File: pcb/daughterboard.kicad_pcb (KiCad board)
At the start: 2 copper layers, 18 parts, among them J1 USB_C_Receptacle_USB2.0, J2 Conn_01x02_Female, J3 Conn_01x02_Female, J4 USB_C_Receptacle_USB2.0, J5 Conn_01x02_Female, J6 Conn_01x02_Female

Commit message: cleanup
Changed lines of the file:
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@@
+    (effects (font (size 0.8 0.8) (thickness 0.15)) (justify mirror))
+  )
+  (gr_text "D-" (at 107.987816 57.802755 -15) (layer "B.SilkS")
     (effects (font (size 0.8 0.8) (thickness 0.15)) (justify mirror))
   )
   (gr_text "D-" (at 68.235 57.678152 -15) (layer "B.SilkS")
+    (effects (font (size 0.8 0.8) (thickness 0.15)) (justify mirror))
+  )
+  (gr_text "D+" (at 106.600608 59.953449 -15) (layer "B.SilkS")
     (effects (font (size 0.8 0.8) (thickness 0.15)) (justify mirror))
   )
@@
     (effects (font (size 0.8 0.8) (thickness 0.15)) (justify mirror))
   )
+  (gr_text "GND" (at 85.778968 58.419 -45) (layer "B.SilkS")
+    (effects (font (size 0.8 0.8) (thickness 0.15)) (justify mirror))
+  )
   (gr_text "Solder on this side" (at 56.16 62.303152) (layer "B.SilkS")
     (effects (font (size 1 1) (thickness 0.2)) (justify mirror))
+  )
+  (gr_text "VBUS" (at 85.55 55.89 -45) (layer "B.SilkS")
+    (effects (font (size 0.8 0.8) (thickness 0.15)) (justify mirror))
+  )
+  (gr_text "GND" (at 85.962816 59.454603 45) (layer "F.SilkS")
+    (effects (font (size 0.8 0.8) (thickness 0.15)))
   )
   (gr_text "Solder on this side" (at 97.61 62.24) (layer "F.SilkS")
@@
     (effects (font (size 1 1) (thickness 0.15)))
   )
+  (gr_text "VBUS" (at 85.733848 56.925603 45) (layer "F.SilkS")
+    (effects (font (size 0.8 0.8) (thickness 0.15)))
+  )
   (gr_text "GND" (at 46.21 59.33 45) (layer "F.SilkS")
     (effects (font (size 0.8 0.8) (thickness 0.15)))
@@
     (effects (font (size 0.8 0.8) (thickness 0.15)))
   )
+  (gr_text "D-" (at 108.312816 58.027755 15) (layer "F.SilkS")
+    (effects (font (size 0.8 0.8) (thickness 0.15)))
+  )
   (gr_text "VBUS" (at 45.981032 56.801 45) (layer "F.SilkS")
     (effects (font (size 0.8 0.8) (thickness 0.15)))
   )
   (gr_text "D+" (at 67.097208 59.978846 15) (layer "F.SilkS")
+    (effects (font (size 0.8 0.8) (thickness 0.15)))
+  )
+  (gr_text "D+" (at 106.850024 60.103449 15) (layer "F.SilkS")
     (effects (font (size 0.8 0.8) (thickness 0.15)))
   )
@@
   (segment (start 57.79 60.47) (end 57.79 58.385) (width 0.16) (layer "F.Cu") (net 7))
   (segment (start 57.88 60.56) (end 57.79 60.47) (width 0.16) (layer "F.Cu") (net 7))
+  (group "" (id 17f6d1cc-928e-464e-bd5a-7a2780c71bd3)
+    (members
+      5be3fcf0-46cd-4786-b369-3cea9f1e6915
+      f567ebe0-93fd-43fa-b74d-07b5c71a5caf
+    )
+  )
+  (group "" (id 2d3d0cfd-134c-4ee0-a173-10009ac37df4)
+    (members
+      0ff945b2-b1c1-42cd-a884-6a1825de5130
+      53c5be92-c0c4-47d7-8633-7af8195c842b
+    )
+  )
+  (group "" (id 2deb0d77-220a-4a1d-b183-9907b7805844)
+    (members
+      1402f9be-3a43-4fa9-94bb-f4ec411d4f4e
+      2cb86200-bc29-4779-b7a9-8bc6408abb5d
+    )
+  )
   (group "" (id 480e8978-8d31-47b8-99c4-efe879f6d8e9)
     (members
@@
     )
   )
+  (group "" (id 90201bdb-25a5-44d0-9fe0-05e41702f812)
+    (members
+      8ecd5bd6-8d66-45c7-bdc6-0ef66b59a163
+      ff73c9f7-4483-4325-aba1-882906f0fa69
+    )
+  )

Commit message: silkscreen. routing
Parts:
- added G***: LOGO, LOGO, F.Cu at (17.0, 88.4)
- added kibuzzard-6284F97C: G***, kibuzzard-6284F97C, F.Cu at (27.6, 80.8)
- added kibuzzard-6284F97C: G***, kibuzzard-6284F97C, F.Cu at (43.3, 86.1)
- added kibuzzard-6284F97C: G***, kibuzzard-6284F97C, F.Cu at (34.4, 83.5)
- added kibuzzard-6284F97C: G***, kibuzzard-6284F97C, F.Cu at (34.4, 78.2)
- added kibuzzard-6284F97C: G***, kibuzzard-6284F97C, F.Cu at (27.6, 86.1)
- added kibuzzard-6284F97C: G***, kibuzzard-6284F97C, F.Cu at (59.0, 86.1)
- added kibuzzard-6284F97C: G***, kibuzzard-6284F97C, F.Cu at (18.7, 83.5)
- added kibuzzard-6284F97C: G***, kibuzzard-6284F97C, F.Cu at (59.0, 80.8)
- added kibuzzard-6284F97C: G***, kibuzzard-6284F97C, F.Cu at (50.1, 78.2)
- added kibuzzard-6284F97C: G***, kibuzzard-6284F97C, F.Cu at (50.1, 83.5)
- added kibuzzard-6284F97C: G***, kibuzzard-6284F97C, F.Cu at (43.3, 80.8)
- moved kibuzzard-6284F97C 41.8 mm to (18.7, 78.2)
- moved kibuzzard-61F01B61 35.2 mm to (42.3, 86.3)
- moved kibuzzard-61F01B61 35.2 mm to (42.1, 86.3)
- moved J1 32.8 mm to (35.0, 81.8)
- moved J2 32.8 mm to (27.3, 81.2)
- moved J3 32.8 mm to (44.5, 81.4)
- moved R2 32.8 mm to (33.7, 85.1)
- moved FB1 29.1 mm to (31.2, 85.2)
- moved R1 27.5 mm to (37.5, 85.3)
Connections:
- J1 pad A1: (no net) -> GND
- J1 pad A12: (no net) -> GND
- J1 pad A4: (no net) -> Net-(J1-PadA4)
- J1 pad A5: (no net) -> Net-(J1-PadA5)
- J1 pad A6: (no net) -> Net-(J1-PadA6)
- J1 pad A7: (no net) -> Net-(J1-PadA7)
- J1 pad A8: (no net) -> unconnected-(J1-PadA8)
- J1 pad A9: (no net) -> Net-(J1-PadA4)
- J1 pad B1: (no net) -> GND
- J1 pad B12: (no net) -> GND
- J1 pad B4: (no net) -> Net-(J1-PadA4)
- J1 pad B5: (no net) -> Net-(J1-PadB5)
- J1 pad B6: (no net) -> Net-(J1-PadA6)
- J1 pad B7: (no net) -> Net-(J1-PadA7)
- J1 pad B8: (no net) -> unconnected-(J1-PadB8)
- J1 pad B9: (no net) -> Net-(J1-PadA4)
- J1 pad S1: (no net) -> Net-(FB1-Pad2)
- J4 pad A1: (no net) -> GND
- J4 pad A12: (no net) -> GND
- J4 pad A4: (no net) -> Net-(J4-PadA4)
- J4 pad A5: (no net) -> Net-(J4-PadA5)
- J4 pad A6: (no net) -> Net-(J4-PadA6)
- J4 pad A7: (no net) -> Net-(J4-PadA7)
- J4 pad A8: (no net) -> unconnected-(J4-PadA8)
- J4 pad A9: (no net) -> Net-(J4-PadA4)
- J4 pad B1: (no net) -> GND
- J4 pad B12: (no net) -> GND
- J4 pad B4: (no net) -> Net-(J4-PadA4)
- J4 pad B5: (no net) -> Net-(J4-PadB5)
- J4 pad B6: (no net) -> Net-(J4-PadA6)
- J4 pad B7: (no net) -> Net-(J4-PadA7)
- J4 pad B8: (no net) -> unconnected-(J4-PadB8)
- J4 pad B9: (no net) -> Net-(J4-PadA4)
- J4 pad S1: (no net) -> Net-(FB2-Pad2)
- J5 pad 1: Net-(J1-PadA4) -> Net-(J4-PadA4)
- J6 pad 1: Net-(J1-PadA7) -> Net-(J4-PadA7)
- J6 pad 2: Net-(J1-PadA6) -> Net-(J4-PadA6)
- R2 pad 1: (no net) -> Net-(J1-PadB5)
- R2 pad 2: (no net) -> GND
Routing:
- net GND: track 4.16 -> 21.4 mm
- net Net-(FB1-Pad2): track 23.9 -> 27.0 mm
- net (no net): track 2.23 -> 0.00 mm
- net Net-(J1-PadB5): track 0.00 -> 1.89 mm
- net Net-(J1-PadA5): track 2.21 -> 2.92 mm
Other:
- board outline added: 21.7 x 12.4 mm

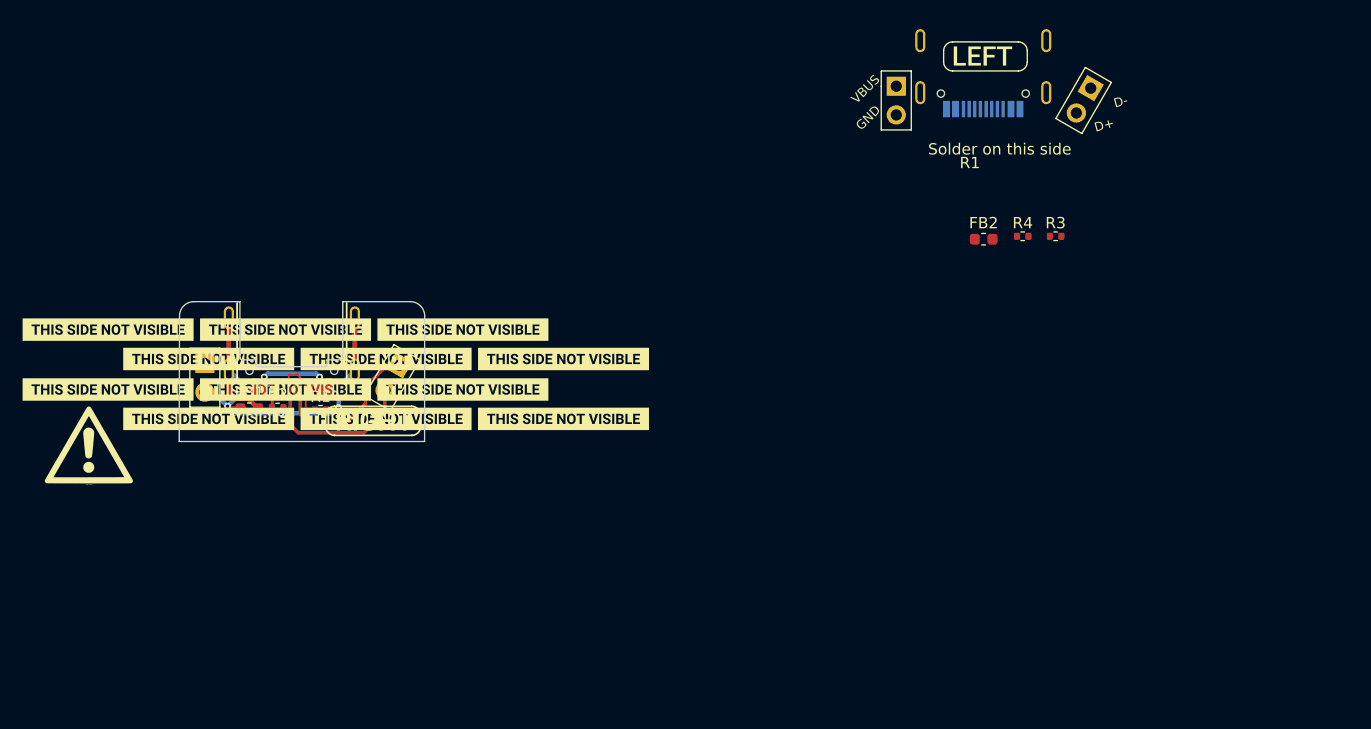
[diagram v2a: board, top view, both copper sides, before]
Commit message: route daughterboards
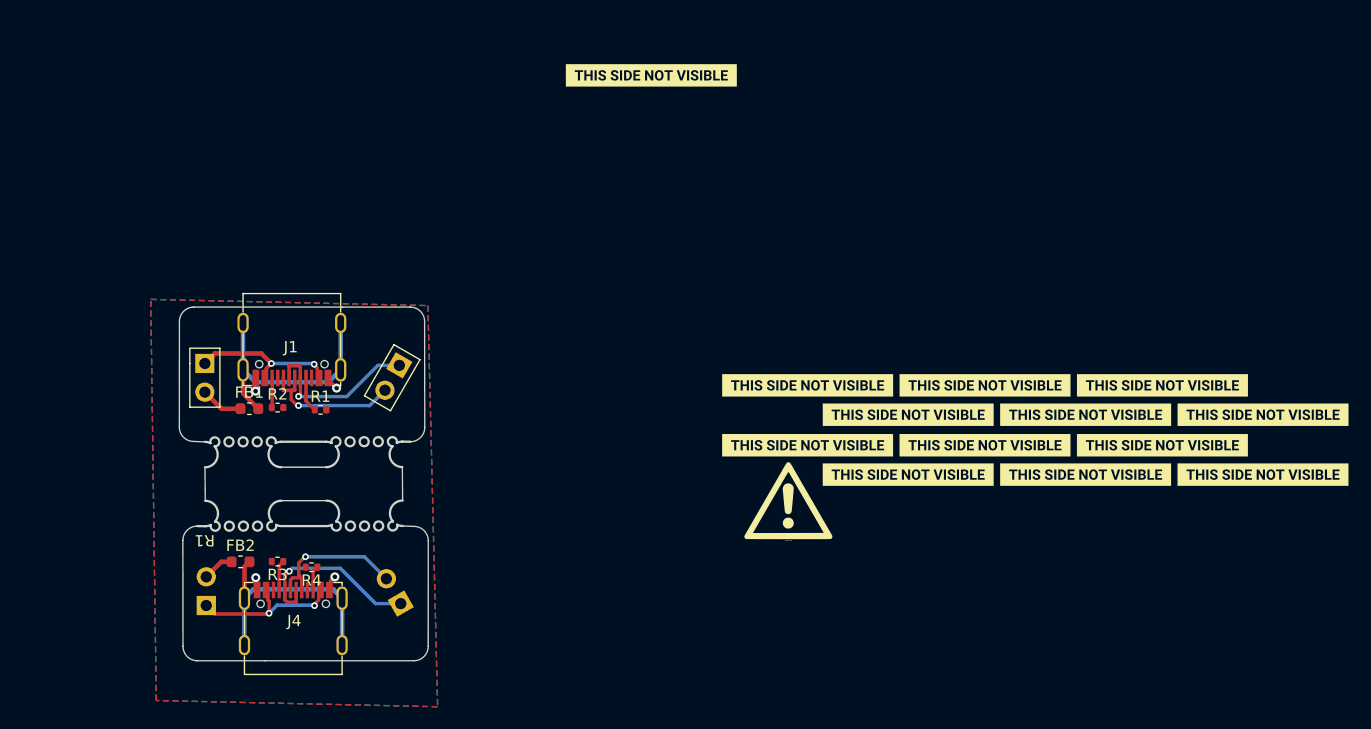
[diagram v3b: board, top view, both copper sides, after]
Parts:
- removed the kibuzzard-61F01B61 at (42.3, 86.3)
- removed kibuzzard-6208EFFE (x2): G***, kibuzzard-6208EFFE
- J1: footprint 0xLib_USB_Type-C:USB_C_Receptacle_HRO_TYPE-C-31-M-14 -> Library:C167321
- J4: footprint 0xLib_USB_Type-C:USB_C_Receptacle_HRO_TYPE-C-31-M-14 -> Library:C167321; moved to F.Cu
- J5, J6: moved to B.Cu
- kibuzzard-6284F97C: moved to F.Cu
- moved J5 76.4 mm to (27.4, 102.6)
- moved J6 76.2 mm to (44.6, 102.4), turned to 30 degrees
- moved J4 75.7 mm to (35.1, 102.0)
- moved R3 74.6 mm to (33.7, 98.7), turned to 180 degrees
- moved FB2 71.7 mm to (30.4, 98.8)
- moved R4 69.4 mm to (36.7, 99.2), turned to 180 degrees
- moved kibuzzard-6284F97C 62.1 mm to (105.2, 85.7)
- moved kibuzzard-6284F97C 62.1 mm to (96.3, 88.4)
- moved kibuzzard-6284F97C 62.1 mm to (96.3, 83.1)
- moved kibuzzard-6284F97C 62.1 mm to (89.5, 91.0)
- moved kibuzzard-6284F97C 62.1 mm to (80.6, 88.4)
- moved kibuzzard-6284F97C 62.1 mm to (120.9, 85.7)
- moved kibuzzard-6284F97C 62.1 mm to (112.0, 83.1)
- moved G*** 62.1 mm to (78.9, 93.3)
- moved kibuzzard-6284F97C 62.1 mm to (105.2, 91.0)
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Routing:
- net Net-(FB2-Pad2): track 0.00 -> 21.0 mm
- net Net-(J4-PadA7): track 0.00 -> 16.1 mm, vias 0 -> 1
- net Net-(J4-PadA4): track 0.00 -> 14.0 mm, vias 0 -> 2
- net Net-(J4-PadA6): track 0.00 -> 13.3 mm, vias 0 -> 1
- net GND: track 21.4 -> 11.5 mm, vias 5 -> 4
- net Net-(J1-PadA4): track 5.15 -> 13.3 mm
- net Net-(FB1-Pad2): track 27.0 -> 21.8 mm
- net Net-(J1-PadA6): track 16.7 -> 13.1 mm, vias 0 -> 1
- net Net-(J1-PadA7): track 17.6 -> 14.9 mm, vias 0 -> 1
- net Net-(J4-PadA5): track 0.00 -> 2.67 mm
- net Net-(J4-PadB5): track 0.00 -> 2.17 mm
- net Net-(J1-PadB5): track 1.89 -> 2.62 mm
- added copper zone on B.Cu, net GND
- added copper zone on F.Cu, net GND
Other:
- board size 21.7 x 12.4 mm -> 22 x 31.3 mm
- board text added: "G"
- board text added: "LEFT"
- board text added: "V"
- board text removed: "GND"
- board text removed: "VBUS"
